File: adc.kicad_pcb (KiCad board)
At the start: 2 copper layers, 17 parts, among them U201 ADS8665IPWR

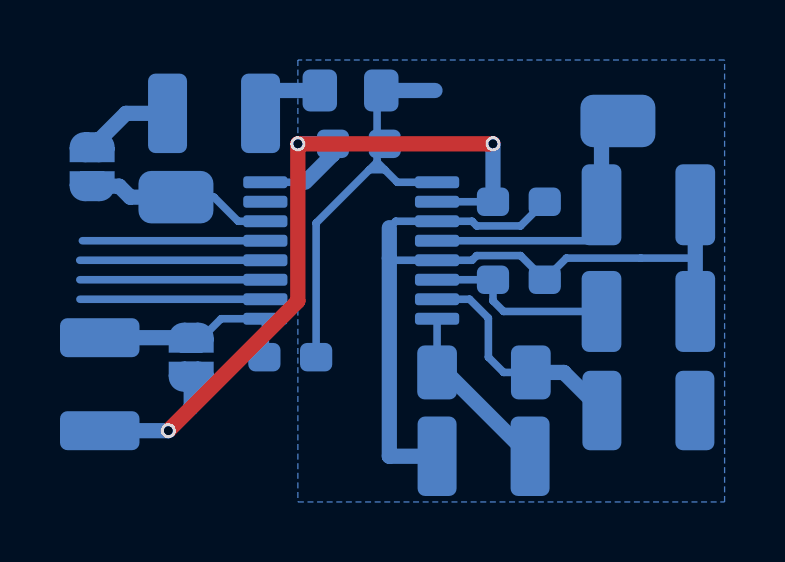
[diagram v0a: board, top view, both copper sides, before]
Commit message: add pcb layout for connection of adc circuit
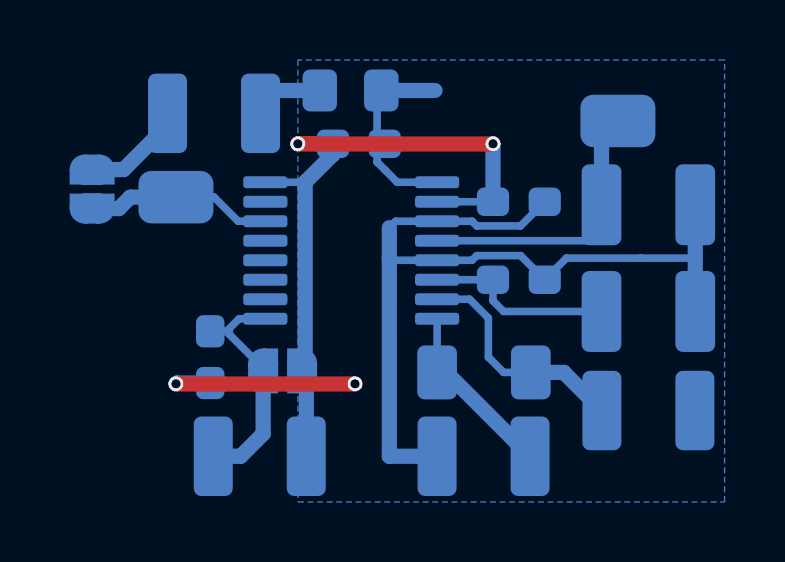
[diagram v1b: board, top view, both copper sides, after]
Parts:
- moved R201 5.85 mm to (72.1, 64.3), turned to 180 degrees
- moved JP201 3.08 mm to (72.9, 61.4), turned to 180 degrees
- moved C201 2.67 mm to (70.5, 61.0), turned to 90 degrees
- moved JP202 0.75 mm to (66.5, 55.4)
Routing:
- net +5VA_adc: track 30.2 -> 23.7 mm, vias 3 -> 2
- net /SCKL: track 6.19 -> 0.00 mm
- net /CONVST/~{CS}: track 6.18 -> 0.00 mm
- net /SDI: track 6.18 -> 0.00 mm
- net /SDO-0: track 6.10 -> 0.00 mm
- net /~{RST}: track 7.08 -> 8.57 mm
- net GND: track 43.7 -> 43.0 mm, vias 0 -> 2
- net /GPO_JMP: track 2.73 -> 3.42 mm
- net /GPO: track 6.78 -> 6.26 mm
